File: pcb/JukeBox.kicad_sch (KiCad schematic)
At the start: 99 parts, among them J1 USB_C_Receptacle_USB2.0_16P, Q1 Q_NPN_BEC, SW1 SW_SPST, SW10 SW_SPST, SW11 SW_SPST, SW12 SW_SPST, SW13 SW_SPST, SW2 SW_SPST, SW3 SW_SPST, SW4 SW_SPST, SW5 SW_SPST, SW6 SW_SPST, SW7 SW_SPST, SW8 SW_SPST, SW9 SW_SPST, U1 NCP1117-3.3_SOT223, U2 W25Q128JVS, U3 RP2350_60QFN, U5 CAT24C512, Y1 ABM8-272-T3

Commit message: DNP updates for BOM
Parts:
- R10, R11, R8, R9: now not fitted
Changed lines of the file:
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@@
 		(in_bom yes)
 		(on_board yes)
-		(dnp no)
+		(dnp yes)
 		(property "Reference" "R10"
 			(at 375.92 205.74 0)
@@
 		(in_bom yes)
 		(on_board yes)
-		(dnp no)
+		(dnp yes)
 		(property "Reference" "R9"
 			(at 355.6 205.74 0)
@@
 		(in_bom yes)
 		(on_board yes)
-		(dnp no)
+		(dnp yes)
 		(property "Reference" "R11"
 			(at 396.24 205.74 0)
@@
 		(in_bom yes)
 		(on_board yes)
-		(dnp no)
+		(dnp yes)
 		(property "Reference" "R8"
 			(at 335.28 205.74 0)

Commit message: update kicad project to kicad 10.0
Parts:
- U4: value ~ -> (none)

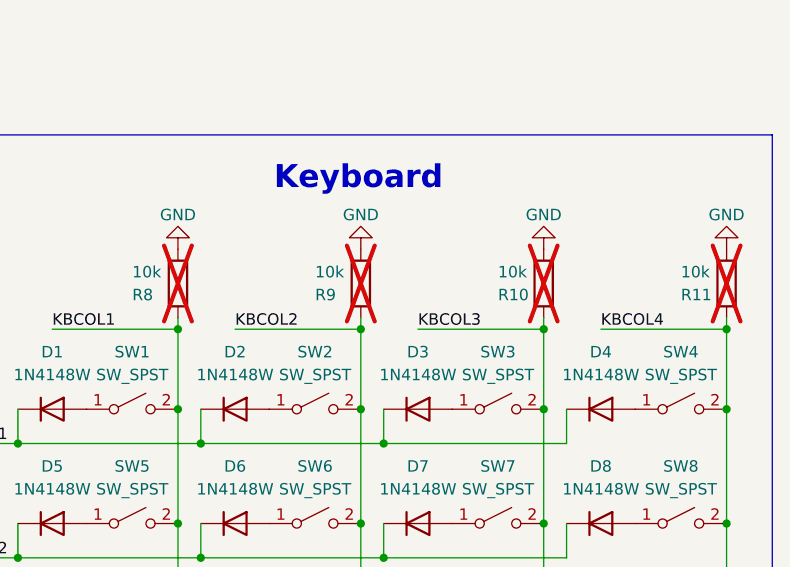
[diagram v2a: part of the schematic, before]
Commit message: fix dnp for key resistors
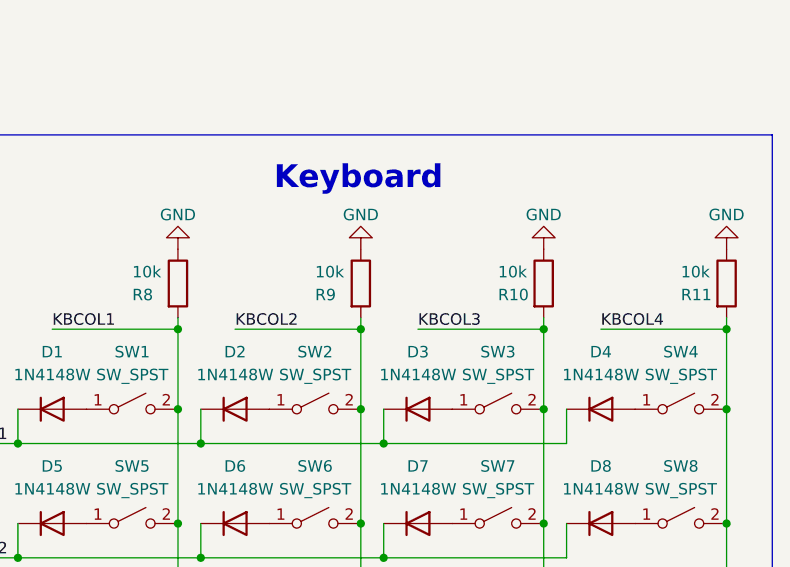
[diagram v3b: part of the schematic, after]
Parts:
- R10, R11, R8, R9: now fitted
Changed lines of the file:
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@@
 		(on_board yes)
 		(in_pos_files yes)
-		(dnp yes)
+		(dnp no)
 		(property "Reference" "R10"
 			(at 375.92 205.74 0)
@@
 		(on_board yes)
 		(in_pos_files yes)
-		(dnp yes)
+		(dnp no)
 		(property "Reference" "R9"
 			(at 355.6 205.74 0)
@@
 		(on_board yes)
 		(in_pos_files yes)
-		(dnp yes)
+		(dnp no)
 		(property "Reference" "R11"
 			(at 396.24 205.74 0)
@@
 		(on_board yes)
 		(in_pos_files yes)
-		(dnp yes)
+		(dnp no)
 		(property "Reference" "R8"
 			(at 335.28 205.74 0)
